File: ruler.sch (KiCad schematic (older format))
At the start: 75 parts, among them J1 USB_OTG, Q1 SOT23, Q2 SOT323, Q3 SOT883, Q4 SOT523, Q5 SOT223, Q6 SOT89, Q7 SuperSOT, SW1 KMR2, SW2 EVQPE1, SW3 B3U1000P, SW4 FSMCT, SW5 TL3315, SW6 FSM2JSM, SW7 JS202011SCQN, SW8 KSR223, U1 QFN-0.5mm, U10 SOT963-6, U11 SSOP14, U12 SO16-L, U13 SOT666, U14 SOT1194, U15 SOT1333, U16 SOT669, U17 TSSOP 4.4x3mm, U18 SO4, U19 VSSOP, U2 LQFP, U3 SOIC, U4 BGA-0.8mm, U5 TSSOP 3x3mm, U6 MSOIC, U7 TSOP-0.95mm, U8 SOT23-6, U9 SOT23-8

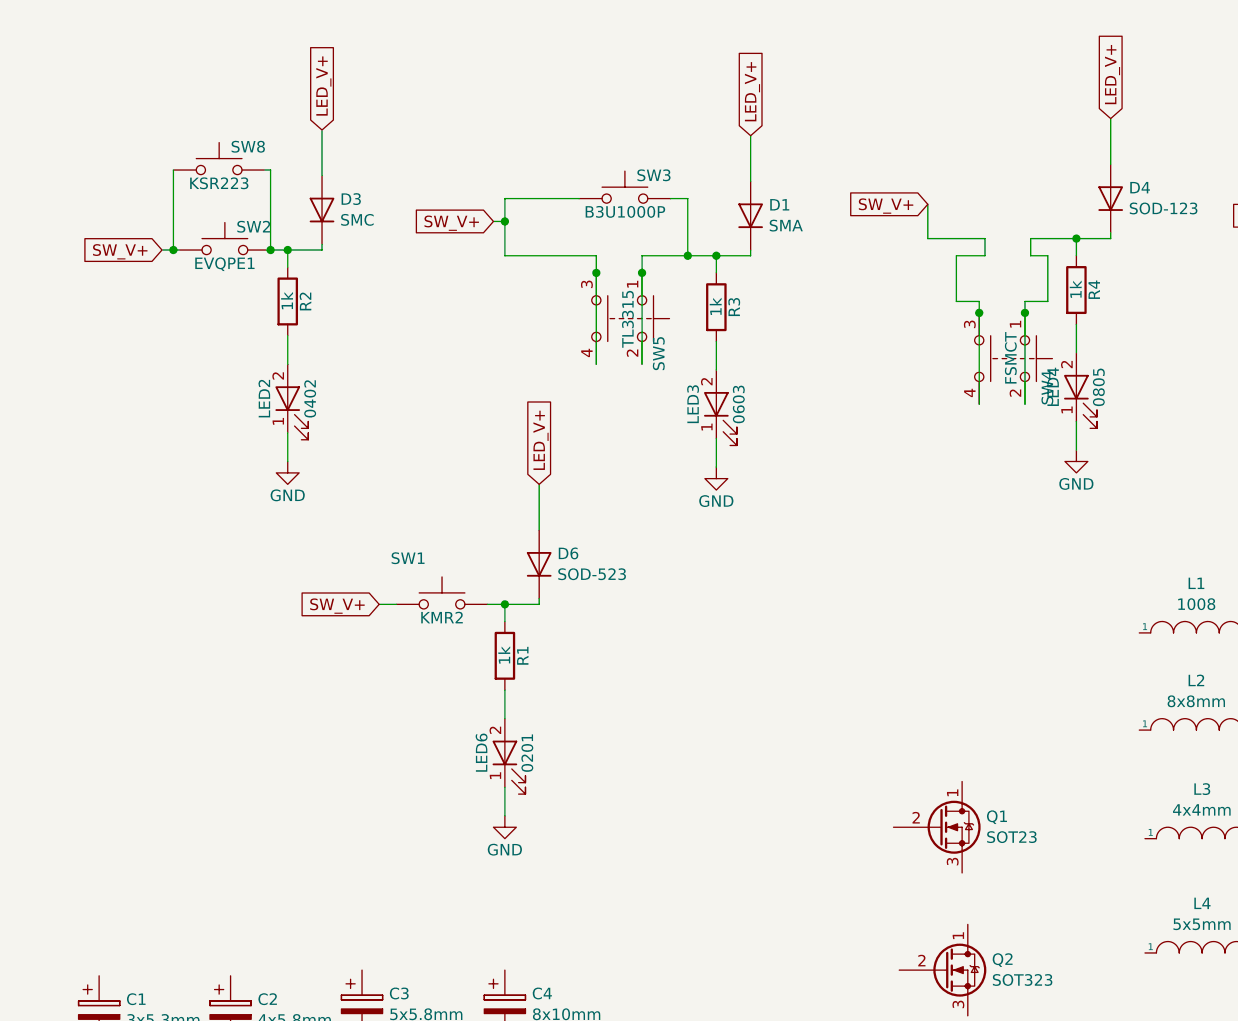
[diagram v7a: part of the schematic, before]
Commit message: Re-arrange buttons
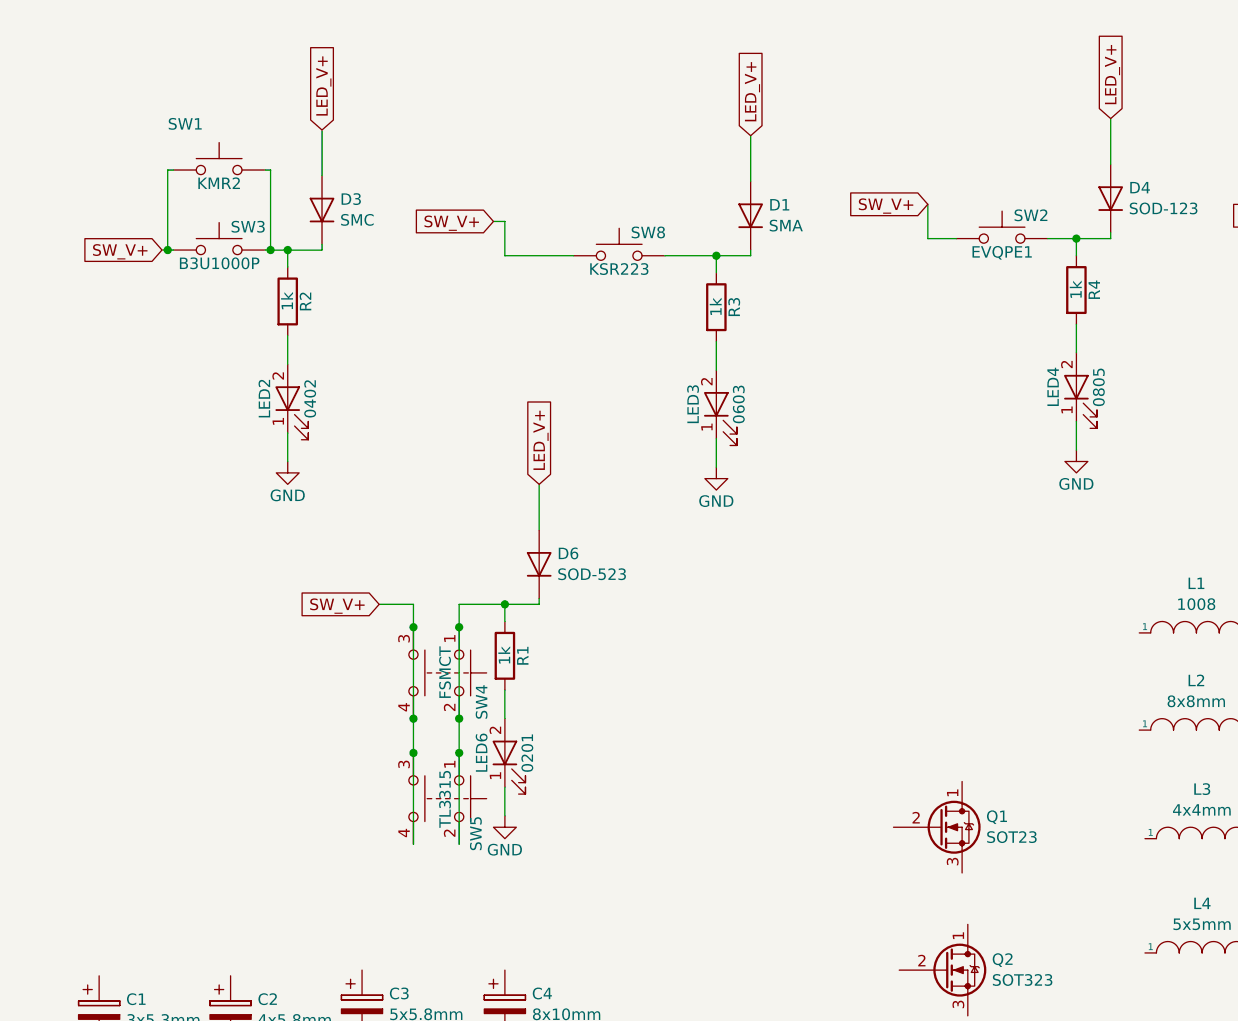
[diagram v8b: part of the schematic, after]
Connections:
- net at D3.1 (K), R2.1: now also SW1.2, SW3.2; no longer SW2.2, SW8.2
- net at SW4.1, SW4.2: now also D6.1 (K), R1.1, SW5.1, SW5.2; no longer D4.1 (K), R4.1
- new net: D1.1 (K), R3.1, SW8.2
- new net: D4.1 (K), R4.1, SW2.2
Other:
- moved on the sheet: SW1, SW2, SW3, SW4, SW5, SW8
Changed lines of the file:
@@
 L ruler-rescue:switches_SW_Push_Dual SW4
 U 1 1 5AF1B6F7
-P 6925 1850
-F 0 "SW4" H 6975 1950 50  0000 L CNN
-F 1 "FSMCT" H 6925 1790 50  0000 C CNN
-F 2 "custom:FSMCT" H 6925 2050 50  0001 C CNN
-F 3 "" H 6925 2050 50  0001 C CNN
-	1    6925 1850
+P 4450 3225
+F 0 "SW4" H 4500 3325 50  0000 L CNN
+F 1 "FSMCT" H 4450 3165 50  0000 C CNN
+F 2 "custom:FSMCT" H 4450 3425 50  0001 C CNN
+F 3 "" H 4450 3425 50  0001 C CNN
+	1    4450 3225
 	0    1    1    0
 $EndComp
@@
 	5575 1400 5575 1475
 $Comp
-L ruler-rescue:switches_SW_Push SW2
-U 1 1 5AF1BC93
-P 3425 1375
-F 0 "SW2" H 3475 1475 50  0000 L CNN
-F 1 "EVQPE1" H 3425 1315 50  0000 C CNN
-F 2 "KiCad/Buttons_Switches_SMD.pretty:SW_SPST_EVQPE1" H 3425 1575 50  0001 C CNN
-F 3 "" H 3425 1575 50  0001 C CNN
-	1    3425 1375
-	1    0    0    -1
-$EndComp
-$Comp
 L ruler-rescue:device_R R4
 U 1 1 5AF1BC99
@@
 L ruler-rescue:switches_SW_Push SW3
 U 1 1 5AF1BCB7
-P 5175 1150
-F 0 "SW3" H 5225 1250 50  0000 L CNN
-F 1 "B3U1000P" H 5175 1090 50  0000 C CNN
-F 2 "digikey/digikey-kicad-library/digikey-footprints.pretty:Switch_Tactile_SMD_B3U-1000P" H 5175 1350 50  0001 C CNN
-F 3 "" H 5175 1350 50  0001 C CNN
-	1    5175 1150
+P 3400 1375
+F 0 "SW3" H 3450 1475 50  0000 L CNN
+F 1 "B3U1000P" H 3400 1315 50  0000 C CNN
+F 2 "digikey/digikey-kicad-library/digikey-footprints.pretty:Switch_Tactile_SMD_B3U-1000P" H 3400 1575 50  0001 C CNN
+F 3 "" H 3400 1575 50  0001 C CNN
+	1    3400 1375
 	1    0    0    -1
 $EndComp
@@
 Text GLabel 3150 1375 0    50   Input ~ 0
 SW_V+
-Wire Wire Line
-	3150 1375 3200 1375
 $Comp
 L ruler-rescue:switches_SW_Push SW1
 U 1 1 5AF21638
-P 4375 2925
-F 0 "SW1" H 4150 3125 50  0000 L CNN
-F 1 "KMR2" H 4375 2865 50  0000 C CNN
-F 2 "KiCad/Buttons_Switches_SMD.pretty:SW_SPST_KMR2" H 4375 3125 50  0001 C CNN
-F 3 "" H 4375 3125 50  0001 C CNN
-	1    4375 2925
-	1    0    0    -1
-$EndComp
-Wire Wire Line
-	4975 1150 4650 1150
-Wire Wire Line
-	4650 1150 4650 1250
+P 3400 1025
+F 0 "SW1" H 3175 1225 50  0000 L CNN
+F 1 "KMR2" H 3400 965 50  0000 C CNN
+F 2 "KiCad/Buttons_Switches_SMD.pretty:SW_SPST_KMR2" H 3400 1225 50  0001 C CNN
+F 3 "" H 3400 1225 50  0001 C CNN
+	1    3400 1025
+	1    0    0    -1
+$EndComp
 Wire Wire Line
 	4600 1250 4650 1250
-Connection ~ 4650 1250
 Wire Wire Line
 	4650 1250 4650 1400
-Wire Wire Line
-	5375 1150 5450 1150
-Wire Wire Line
-	5450 1150 5450 1400
-Connection ~ 5450 1400
-Wire Wire Line
-	5450 1400 5575 1400
 Text GLabel 3850 850  1    50   Input ~ 0
 LED_V+
-Wire Wire Line
-	3200 1025 3200 1375
-Connection ~ 3200 1375
 Wire Wire Line
 	3625 1375 3625 1025
@@
 Wire Wire Line
 	7300 1325 7150 1325
-Connection ~ 7150 1325
 Text GLabel 9075 950  1    50   Input ~ 0
 LED_V+
@@
 	0    -1   -1   0
 $EndComp
-Wire Wire Line
-	3225 1375 3200 1375
 $Comp
 L ruler-rescue:switches_SW_Push SW6
@@
 L ruler-rescue:switches_SW_Push_Dual SW5
 U 1 1 5AF1AB0F
-P 5250 1675
-F 0 "SW5" H 5325 1750 50  0000 L CNN
-F 1 "TL3315" H 5250 1615 50  0000 C CNN
-F 2 "digikey/digikey-kicad-library/digikey-footprints.pretty:Switch_4.5x4.5mm_SMD_TL3315NF160Q" H 5250 1875 50  0001 C CNN
-F 3 "" H 5250 1875 50  0001 C CNN
-	1    5250 1675
+P 4450 3775
+F 0 "SW5" H 4525 3850 50  0000 L CNN
+F 1 "TL3315" H 4450 3715 50  0000 C CNN
+F 2 "digikey/digikey-kicad-library/digikey-footprints.pretty:Switch_4.5x4.5mm_SMD_TL3315NF160Q" H 4450 3975 50  0001 C CNN
+F 3 "" H 4450 3975 50  0001 C CNN
+	1    4450 3775
 	0    1    1    0
 $EndComp
 Wire Wire Line
-	4650 1400 5050 1400
-Wire Wire Line
-	5250 1400 5450 1400
-Wire Wire Line
-	5050 1400 5050 1475
-Connection ~ 5050 1475
-Wire Wire Line
-	5050 1475 5050 1875
-Wire Wire Line
-	5250 1400 5250 1475
-Connection ~ 5250 1475
-Wire Wire Line
-	5250 1475 5250 1875
-Wire Wire Line
-	6500 1325 6750 1325
-Wire Wire Line
-	6950 1325 7150 1325
-Wire Wire Line
-	6750 1325 6750 1400
-Wire Wire Line
-	6950 1325 6950 1400
-Wire Wire Line
-	6750 1400 6625 1400
-Wire Wire Line
-	6625 1400 6625 1600
+	6500 1325 6625 1325
 Wire Wire Line
 	7150 1700 7150 1825
-Wire Wire Line
-	6950 1400 7025 1400
-Wire Wire Line
-	7025 1400 7025 1600
-Wire Wire Line
-	6725 1650 6725 2050
-Wire Wire Line
-	6925 1650 6925 2050
-Wire Wire Line
-	6625 1600 6725 1600
-Wire Wire Line
-	6725 1600 6725 1650
-Connection ~ 6725 1650
-Wire Wire Line
-	6925 1650 6925 1600
-Wire Wire Line
-	6925 1600 7025 1600
-Connection ~ 6925 1650
 $Comp
 L ruler-rescue:conn_Conn_01x01 U1
@@
 L ruler-rescue:switches_SW_Push SW8
 U 1 1 5B70AFF0
-P 3400 1025
-F 0 "SW8" H 3450 1125 50  0000 L CNN
-F 1 "KSR223" H 3400 965 50  0000 C CNN
-F 2 "OpenMusicKontrollers/omk.pretty:KSR" H 3400 1225 50  0001 C CNN
-F 3 "" H 3400 1225 50  0001 C CNN
-	1    3400 1025
+P 5150 1400
+F 0 "SW8" H 5200 1500 50  0000 L CNN
+F 1 "KSR223" H 5150 1340 50  0000 C CNN
+F 2 "OpenMusicKontrollers/omk.pretty:KSR" H 5150 1600 50  0001 C CNN
+F 3 "" H 5150 1600 50  0001 C CNN
+	1    5150 1400
 	1    0    0    -1
 $EndComp
@@
 LED_V+
 Wire Wire Line
-	4575 2925 4650 2925
-Wire Wire Line
 	4800 2400 4800 2600
 Wire Wire Line
@@
 	4650 3300 4650 3425
 Wire Wire Line
-	4100 2925 4175 2925
+	7025 1325 7150 1325
+Connection ~ 7150 1325
+Wire Wire Line
+	3600 1375 3625 1375
+Wire Wire Line
+	3200 1375 3175 1375
+Wire Wire Line
+	3175 1375 3175 1025
+Wire Wire Line
+	3175 1025 3200 1025
+Connection ~ 3175 1375
+Wire Wire Line
+	3175 1375 3150 1375
+Wire Wire Line
+	4100 2925 4250 2925
+Wire Wire Line
+	4250 2925 4250 3025
+Connection ~ 4250 3025
+Wire Wire Line
+	4250 3025 4250 3425
+Wire Wire Line
+	4450 3425 4450 3025
+Wire Wire Line
+	4450 2925 4650 2925
+Connection ~ 4450 3025
+Wire Wire Line
+	4450 3025 4450 2925
+Connection ~ 4250 3425
+Connection ~ 4450 3425
+Wire Wire Line
+	4250 3425 4250 3575
+Connection ~ 4250 3575
+Wire Wire Line
+	4250 3575 4250 3975
+Wire Wire Line
+	4450 3425 4450 3575
+Connection ~ 4450 3575
+Wire Wire Line
+	4450 3575 4450 3975
+Wire Wire Line
+	4650 1400 4950 1400
+$Comp
+L ruler-rescue:switches_SW_Push SW2
+U 1 1 5AF1BC93
+P 6825 1325
+F 0 "SW2" H 6875 1425 50  0000 L CNN
+F 1 "EVQPE1" H 6825 1265 50  0000 C CNN
+F 2 "KiCad/Buttons_Switches_SMD.pretty:SW_SPST_EVQPE1" H 6825 1525 50  0001 C CNN
+F 3 "" H 6825 1525 50  0001 C CNN
+	1    6825 1325
+	1    0    0    -1
+$EndComp
+Wire Wire Line
+	5350 1400 5575 1400
 $EndSCHEMATC
